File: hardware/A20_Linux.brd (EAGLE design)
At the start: 160 x 100 mm, 54 parts, among them U1 A20, U2 H5TQ4G63MFR, U3 H5TQ4G63MFR, U4 H27UBG8T2BTR

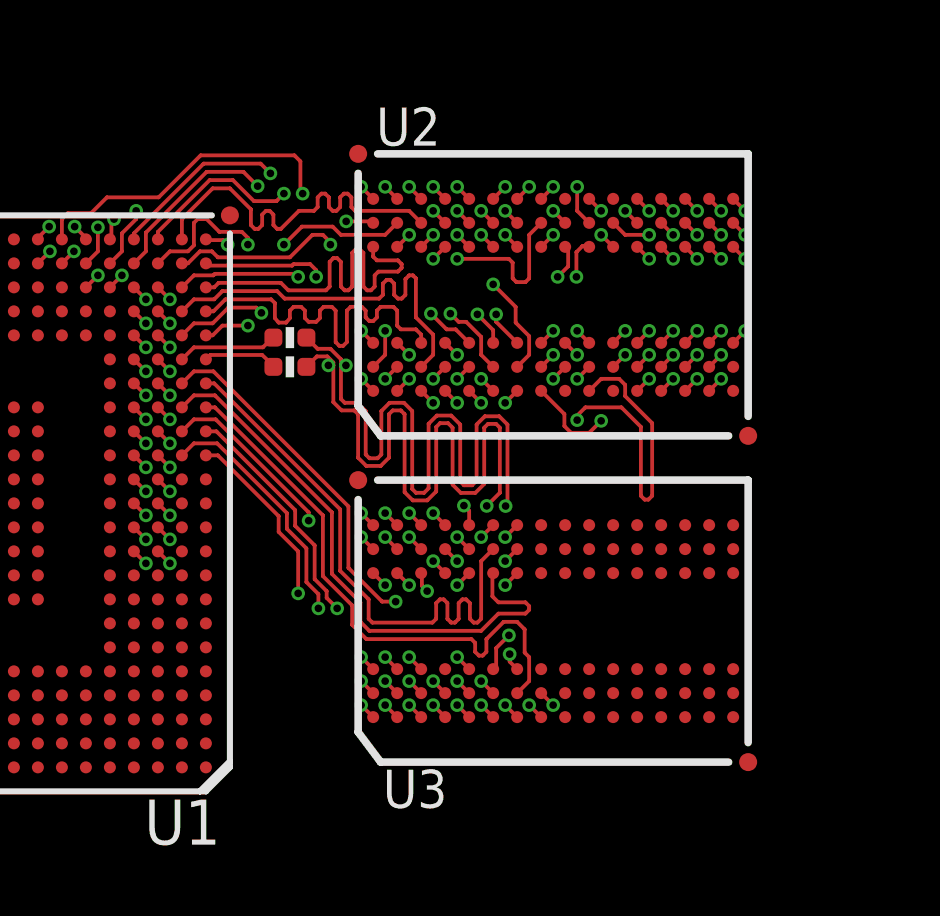
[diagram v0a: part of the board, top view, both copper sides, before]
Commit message: More Routing
Added more DDR3 routing on the PCB
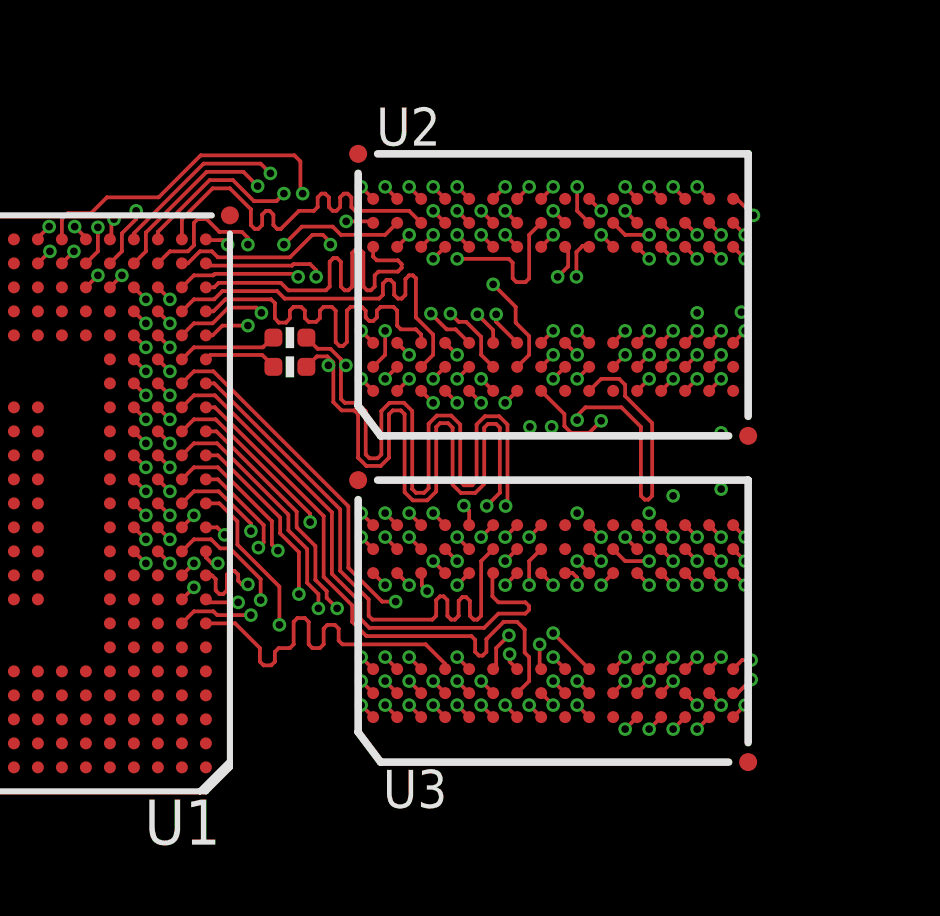
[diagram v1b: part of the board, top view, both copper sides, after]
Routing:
- net !CAS: track 1.13 -> 33.1 mm, vias 2 -> 4
- net !RAS: track 1.13 -> 29.5 mm, vias 2 -> 4
- net CKE: track 1.13 -> 28.0 mm, vias 2 -> 4
- net DDR_VREF: track 4.11 -> 25.3 mm, vias 3 -> 4
- net BA1: track 1.13 -> 20.2 mm, vias 2 -> 4
- net BA0: track 1.13 -> 18.7 mm, vias 2 -> 4
- net SA8: track 1.13 -> 18.2 mm, vias 2 -> 4
- net SA4: track 1.13 -> 18.1 mm, vias 2 -> 4
- net SA6: track 1.13 -> 16.4 mm, vias 2 -> 4
- net SA7: track 1.13 -> 15.2 mm, vias 2 -> 4
- net SDQM3: track 0.00 -> 12.5 mm
- net DDR3_ODT: track 11.5 -> 22.4 mm, vias 2 -> 3
- net DQ29: track 0.57 -> 5.89 mm, vias 1 -> 2
- net DQ18: track 0.57 -> 5.53 mm, vias 1 -> 2
- net GND: track 18.7 -> 23.0 mm, vias 33 -> 40
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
